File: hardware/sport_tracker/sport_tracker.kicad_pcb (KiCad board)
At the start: 2 copper layers, 24 x 16 mm, 20 parts, among them J1 USB-C, SW1 BTN, U1 ESP32-C3FN4, U2 QMI8658C, U3 TP4054

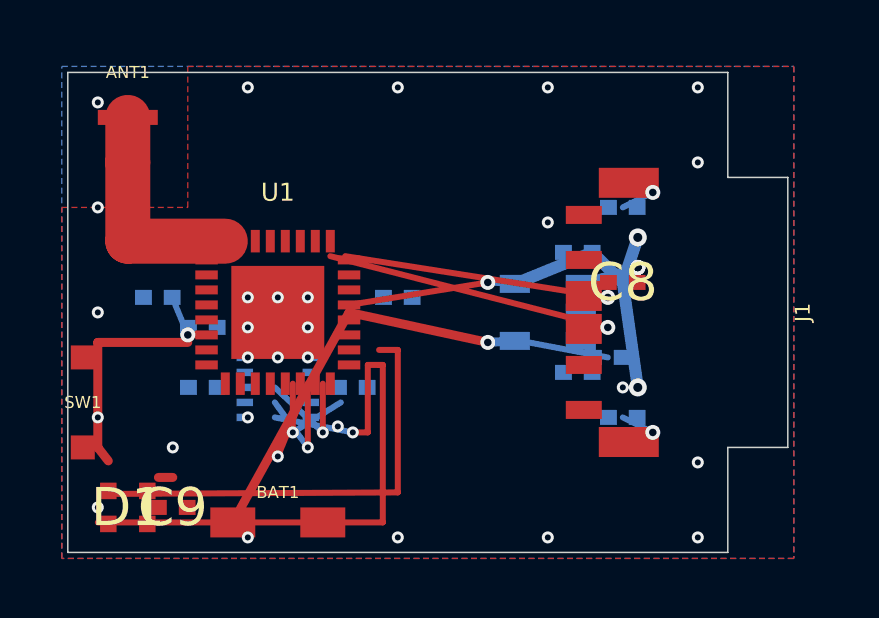
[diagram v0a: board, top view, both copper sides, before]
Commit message: Final PCB: USB-C fully inside board, all 18 nets routed
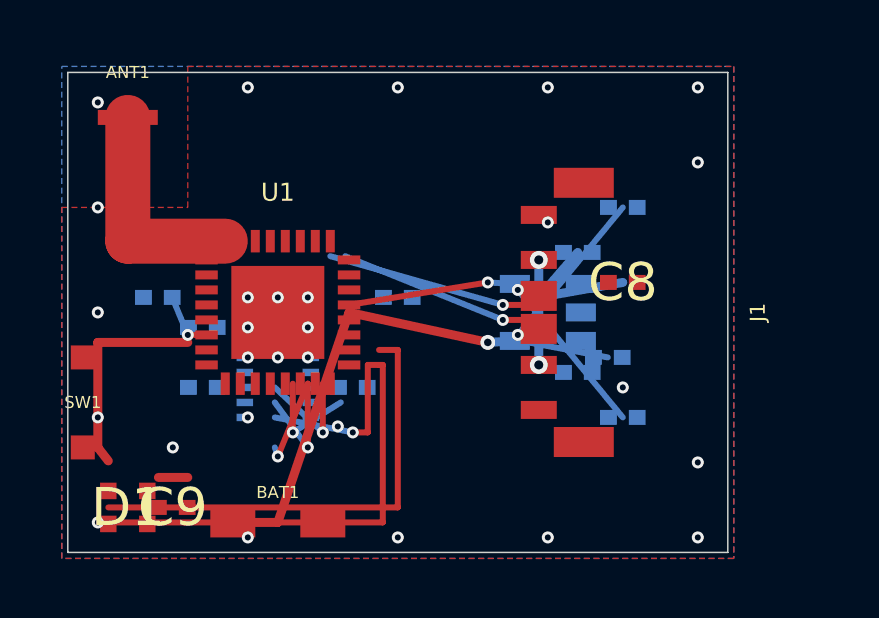
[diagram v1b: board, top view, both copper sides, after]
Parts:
- moved J1 1.50 mm to (107.5, 100.0)
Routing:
- net CC2: track 1.12 -> 6.21 mm
- net CC1: track 1.12 -> 6.21 mm
- net CHRG_STAT: track 8.27 -> 5.59 mm, vias 4 -> 1
- net USB_DM: track 9.55 -> 7.18 mm
- net USB_DP: track 8.86 -> 6.86 mm
- net VBAT: track 21.2 -> 22.6 mm
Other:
- board size 24 x 16 mm -> 22 x 16 mm

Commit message: Update U1->ESP32-C3FH4, U2->QMI8658A (availability fix)
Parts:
- U1: value ESP32-C3FN4 -> ESP32-C3FH4
- U2: value QMI8658C -> QMI8658A
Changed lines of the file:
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@@
 			)
 		)
-		(property "Value" "ESP32-C3FN4"
+		(property "Value" "ESP32-C3FH4"
 			(at 0 4 0)
 			(layer "F.Fab")
@@
 			)
 		)
-		(property "Value" "QMI8658C"
+		(property "Value" "QMI8658A"
 			(at 0 2.5 0)
 			(layer "B.Fab")
